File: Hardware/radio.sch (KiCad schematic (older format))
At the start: 4 parts

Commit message: Connected radio to ESP32
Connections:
- net labels added: SCLK
- net labels removed: SCK
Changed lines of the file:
@@
 	5400 3650 5250 3650
 Text HLabel 5250 3650 0    50   Input ~ 0
-SCK
+SCLK
 Text HLabel 5250 3750 0    50   Input ~ 0
 MOSI
@@
 	5900 4550 5900 4650
 $Comp
-L power:GND #PWR?
+L power:GND #PWR0106
 U 1 1 606C4DD1
 P 5900 4650
-F 0 "#PWR?" H 5900 4400 50  0001 C CNN
+F 0 "#PWR0106" H 5900 4400 50  0001 C CNN
 F 1 "GND" H 5905 4477 50  0000 C CNN
 F 2 "" H 5900 4650 50  0001 C CNN
@@
 	6800 3850 6800 3950
 $Comp
-L power:GND #PWR?
+L power:GND #PWR0107
 U 1 1 606C9E63
 P 6800 3950
-F 0 "#PWR?" H 6800 3700 50  0001 C CNN
+F 0 "#PWR0107" H 6800 3700 50  0001 C CNN
 F 1 "GND" H 6805 3777 50  0000 C CNN
 F 2 "" H 6800 3950 50  0001 C CNN
@@
 $EndComp
 $Comp
-L power:+3V3 #PWR?
+L power:+3V3 #PWR0108
 U 1 1 606D3D70
 P 5900 2750
-F 0 "#PWR?" H 5900 2600 50  0001 C CNN
+F 0 "#PWR0108" H 5900 2600 50  0001 C CNN
 F 1 "+3V3" H 5915 2923 50  0000 C CNN
 F 2 "" H 5900 2750 50  0001 C CNN
@@
 $EndComp
 $Comp
-L power:GND #PWR?
+L power:GND #PWR0109
 U 1 1 606DD712
 P 6300 3000
-F 0 "#PWR?" H 6300 2750 50  0001 C CNN
+F 0 "#PWR0109" H 6300 2750 50  0001 C CNN
 F 1 "GND" V 6305 2872 50  0000 R CNN
 F 2 "" H 6300 3000 50  0001 C CNN

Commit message: Switched antenna from SMA connector to through-hole
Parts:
- removed J?: Conn_Coaxial, symbol Connector:Conn_Coaxial
- added AE?: Antenna, symbol Device:Antenna
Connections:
- wire segments 20 -> 19
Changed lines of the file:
@@
 	1    0    0    -1
 $EndComp
-$Comp
-L Connector:Conn_Coaxial J?
-U 1 1 606C8A45
-P 6800 3650
-F 0 "J?" H 6900 3625 50  0000 L CNN
-F 1 "Conn_Coaxial" H 6900 3534 50  0000 L CNN
-F 2 "" H 6800 3650 50  0001 C CNN
-F 3 " ~" H 6800 3650 50  0001 C CNN
-	1    6800 3650
-	1    0    0    -1
-$EndComp
-Wire Wire Line
-	6800 3850 6800 3950
-$Comp
-L power:GND #PWR0107
-U 1 1 606C9E63
-P 6800 3950
-F 0 "#PWR0107" H 6800 3700 50  0001 C CNN
-F 1 "GND" H 6805 3777 50  0000 C CNN
-F 2 "" H 6800 3950 50  0001 C CNN
-F 3 "" H 6800 3950 50  0001 C CNN
-	1    6800 3950
-	1    0    0    -1
-$EndComp
-Wire Wire Line
-	6400 3650 6600 3650
 Wire Wire Line
 	5400 4150 5250 4150
@@
 Wire Wire Line
 	6300 3000 6300 2850
+Wire Wire Line
+	6400 3650 6650 3650
+$Comp
+L Device:Antenna AE?
+U 1 1 606E40D7
+P 6850 3650
+F 0 "AE?" V 6804 3780 50  0000 L CNN
+F 1 "Antenna" V 6895 3780 50  0000 L CNN
+F 2 "" H 6850 3650 50  0001 C CNN
+F 3 "~" H 6850 3650 50  0001 C CNN
+	1    6850 3650
+	0    1    1    0
+$EndComp
 $EndSCHEMATC

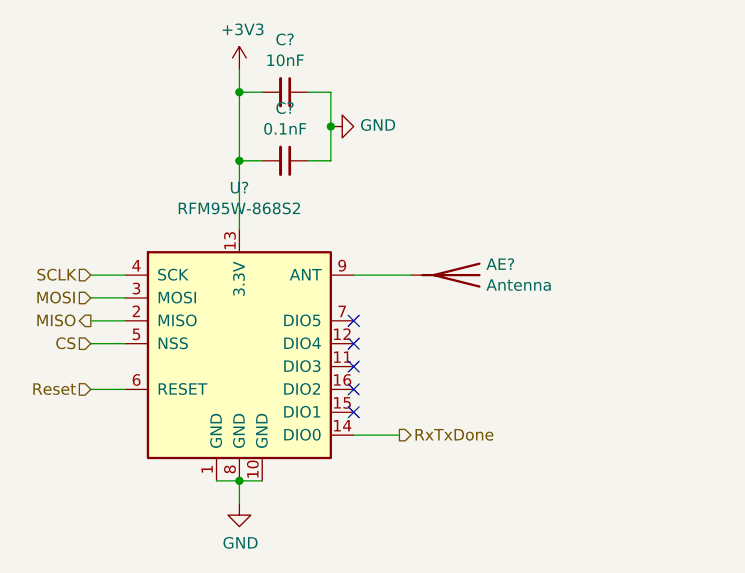
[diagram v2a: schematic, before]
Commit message: Added comment about decoupling capacitors
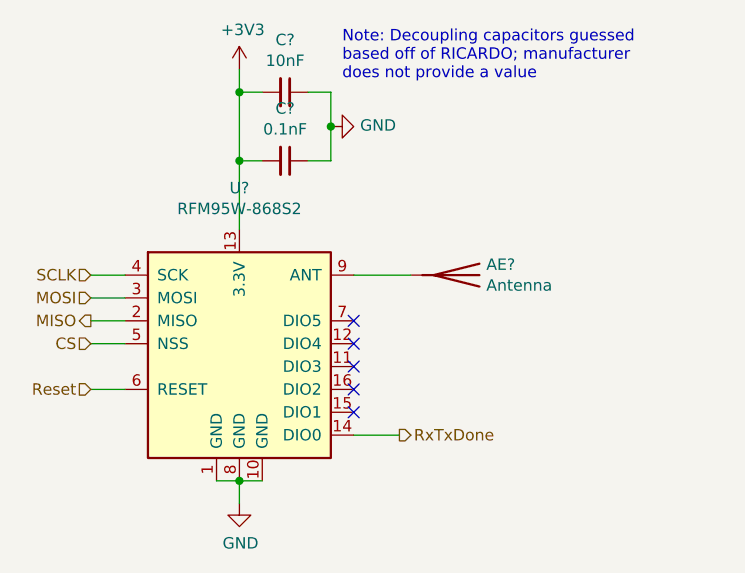
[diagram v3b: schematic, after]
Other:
- note added: "Note: Decoupling capacitors guessed\nbased off of RICARDO; manufacturer\ndoes not provide a value"
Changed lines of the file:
@@
 	0    1    1    0
 $EndComp
+Text Notes 6350 2800 0    50   ~ 0
+Note: Decoupling capacitors guessed\nbased off of RICARDO; manufacturer\ndoes not provide a value
 $EndSCHEMATC
